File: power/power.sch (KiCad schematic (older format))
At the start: 69 parts, among them J1 Conn_01x02_Female, J10 Conn_01x02_Female, J11 Conn_01x02_Female, J12 Conn_01x02_Female, J13 Conn_01x02_Female, J14 Conn_01x02_Female, J15 Conn_01x03_Male, J2 Barrel_jack, J3 Conn_01x02_Female, J4 Conn_01x02_Female, J5 CONN_02X03, J6 Conn_01x02_Female, J7 Conn_01x02_Female, J8 Conn_01x02_Female, J9 Conn_01x02_Female, Q1 BS170, Q2 BS170, Q3 BS170, Q4 BS170, Q5 BS170, Q6 BS170, U1 ATMEGA16M1, U2 TPS2592xx, U3 LP5907MFX-3_3_NOPB

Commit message: final rev 1: nickel pads added and recovery footprint issues fixed
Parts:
- J1, J3, J4, J6, J7, J8: footprint Connector_PinHeader_1.00mm:PinHeader_1x02_P1.00mm_Vertical -> footprints:nickel_pad_bms
- sol1, sol2: footprint recovery-trigger-sp20:OSTTC030162 -> footprints:OSTTC030162
- tres1sol1, tres1sol2: footprint recovery-trigger-sp20:CSD16322Q5 -> footprints:TRANS_CSD17312Q5
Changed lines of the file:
@@
 F 0 "J1" H 5417 3116 50  0000 L CNN
 F 1 "Conn_01x02_Female" H 5417 3025 50  0000 L CNN
-F 2 "Connector_PinHeader_1.00mm:PinHeader_1x02_P1.00mm_Vertical" H 5390 3140 50  0001 C CNN
+F 2 "footprints:nickel_pad_bms" H 5390 3140 50  0001 C CNN
 F 3 "~" H 5390 3140 50  0001 C CNN
 	1    5390 3140
@@
 F 0 "J3" H 5427 3366 50  0000 L CNN
 F 1 "Conn_01x02_Female" H 5427 3275 50  0000 L CNN
-F 2 "Connector_PinHeader_1.00mm:PinHeader_1x02_P1.00mm_Vertical" H 5400 3390 50  0001 C CNN
+F 2 "footprints:nickel_pad_bms" H 5400 3390 50  0001 C CNN
 F 3 "~" H 5400 3390 50  0001 C CNN
 	1    5400 3390
@@
 F 0 "J4" H 5427 3606 50  0000 L CNN
 F 1 "Conn_01x02_Female" H 5427 3515 50  0000 L CNN
-F 2 "Connector_PinHeader_1.00mm:PinHeader_1x02_P1.00mm_Vertical" H 5400 3630 50  0001 C CNN
+F 2 "footprints:nickel_pad_bms" H 5400 3630 50  0001 C CNN
 F 3 "~" H 5400 3630 50  0001 C CNN
 	1    5400 3630
@@
 F 0 "J6" H 6277 3136 50  0000 L CNN
 F 1 "Conn_01x02_Female" H 6277 3045 50  0000 L CNN
-F 2 "Connector_PinHeader_1.00mm:PinHeader_1x02_P1.00mm_Vertical" H 6250 3160 50  0001 C CNN
+F 2 "footprints:nickel_pad_bms" H 6250 3160 50  0001 C CNN
 F 3 "~" H 6250 3160 50  0001 C CNN
 	1    6250 3160
@@
 F 0 "J7" H 6287 3376 50  0000 L CNN
 F 1 "Conn_01x02_Female" H 6287 3285 50  0000 L CNN
-F 2 "Connector_PinHeader_1.00mm:PinHeader_1x02_P1.00mm_Vertical" H 6260 3400 50  0001 C CNN
+F 2 "footprints:nickel_pad_bms" H 6260 3400 50  0001 C CNN
 F 3 "~" H 6260 3400 50  0001 C CNN
 	1    6260 3400
@@
 F 0 "J8" H 6287 3616 50  0000 L CNN
 F 1 "Conn_01x02_Female" H 6287 3525 50  0000 L CNN
-F 2 "Connector_PinHeader_1.00mm:PinHeader_1x02_P1.00mm_Vertical" H 6260 3640 50  0001 C CNN
+F 2 "footprints:nickel_pad_bms" H 6260 3640 50  0001 C CNN
 F 3 "~" H 6260 3640 50  0001 C CNN
 	1    6260 3640
@@
 F 0 "sol1" H 10172 2915 59  0000 C CNN
 F 1 "OSTTC03" H 10172 2810 59  0000 C CNN
-F 2 "recovery-trigger-sp20:OSTTC030162" H 10089 2669 59  0001 C CNN
+F 2 "footprints:OSTTC030162" H 10089 2669 59  0001 C CNN
 F 3 "http://www.on-shore.com/wp-content/uploads/OSTTCXX0162.pdf" H 10089 2669 59  0001 C CNN
 F 4 "https://www.digikey.com/product-detail/en/on-shore-technology-inc/OSTTC030162/ED2601-ND/614550" H 10189 2969 59  0001 C CNN "Purchasing Link"
@@
 F 0 "tres1sol1" H 13885 1394 50  0000 C CNN
 F 1 "NMOS_CDS16" H 13885 1303 50  0000 C CNN
-F 2 "recovery-trigger-sp20:CSD16322Q5" H 13085 1329 50  0001 C CNN
+F 2 "footprints:TRANS_CSD17312Q5" H 13085 1329 50  0001 C CNN
 F 3 "http://www.ti.com/general/docs/suppproductinfo.tsp?distId=10&gotoUrl=http%3A%2F%2Fwww.ti.com%2Flit%2Fgpn%2Fcsd16322q5" H 13985 1479 50  0001 C CNN
 F 4 "CSD16322Q5" H 14085 1629 50  0001 C CNN "MPN"
@@
 F 0 "tres1sol2" H 13936 3021 50  0000 C CNN
 F 1 "NMOS_CDS16" H 13936 2930 50  0000 C CNN
-F 2 "recovery-trigger-sp20:CSD16322Q5" H 13136 2956 50  0001 C CNN
+F 2 "footprints:TRANS_CSD17312Q5" H 13136 2956 50  0001 C CNN
 F 3 "http://www.ti.com/general/docs/suppproductinfo.tsp?distId=10&gotoUrl=http%3A%2F%2Fwww.ti.com%2Flit%2Fgpn%2Fcsd16322q5" H 14036 3106 50  0001 C CNN
 F 4 "CSD16322Q5" H 14136 3256 50  0001 C CNN "MPN"
@@
 F 0 "sol2" H 11374 2919 59  0000 C CNN
 F 1 "OSTTC03" H 11374 2814 59  0000 C CNN
-F 2 "recovery-trigger-sp20:OSTTC030162" H 11291 2673 59  0001 C CNN
+F 2 "footprints:OSTTC030162" H 11291 2673 59  0001 C CNN
 F 3 "http://www.on-shore.com/wp-content/uploads/OSTTCXX0162.pdf" H 11291 2673 59  0001 C CNN
 F 4 "https://www.digikey.com/product-detail/en/on-shore-technology-inc/OSTTC030162/ED2601-ND/614550" H 11391 2973 59  0001 C CNN "Purchasing Link"

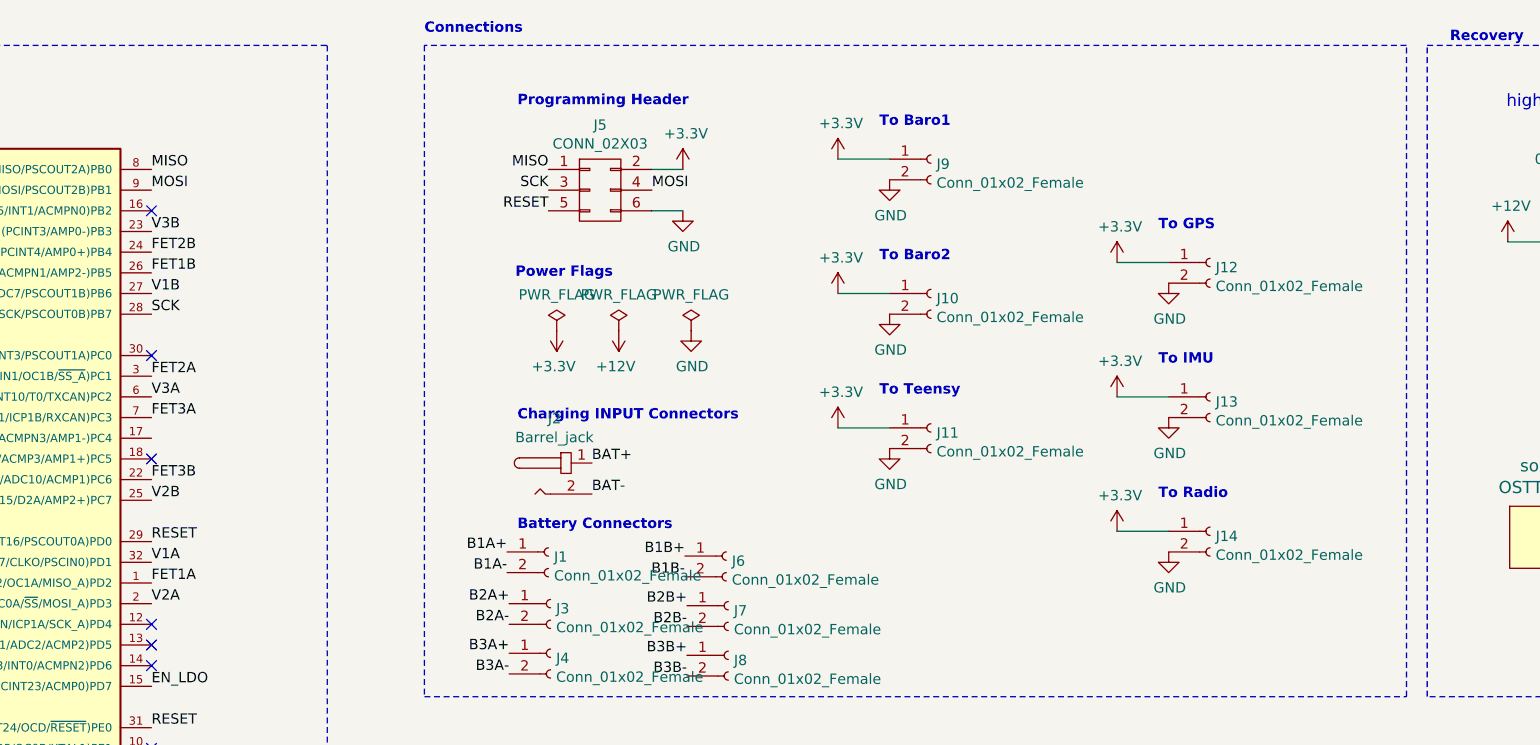
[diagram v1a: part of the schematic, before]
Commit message: ribbon added to sch and recovery wires increased and no connects added
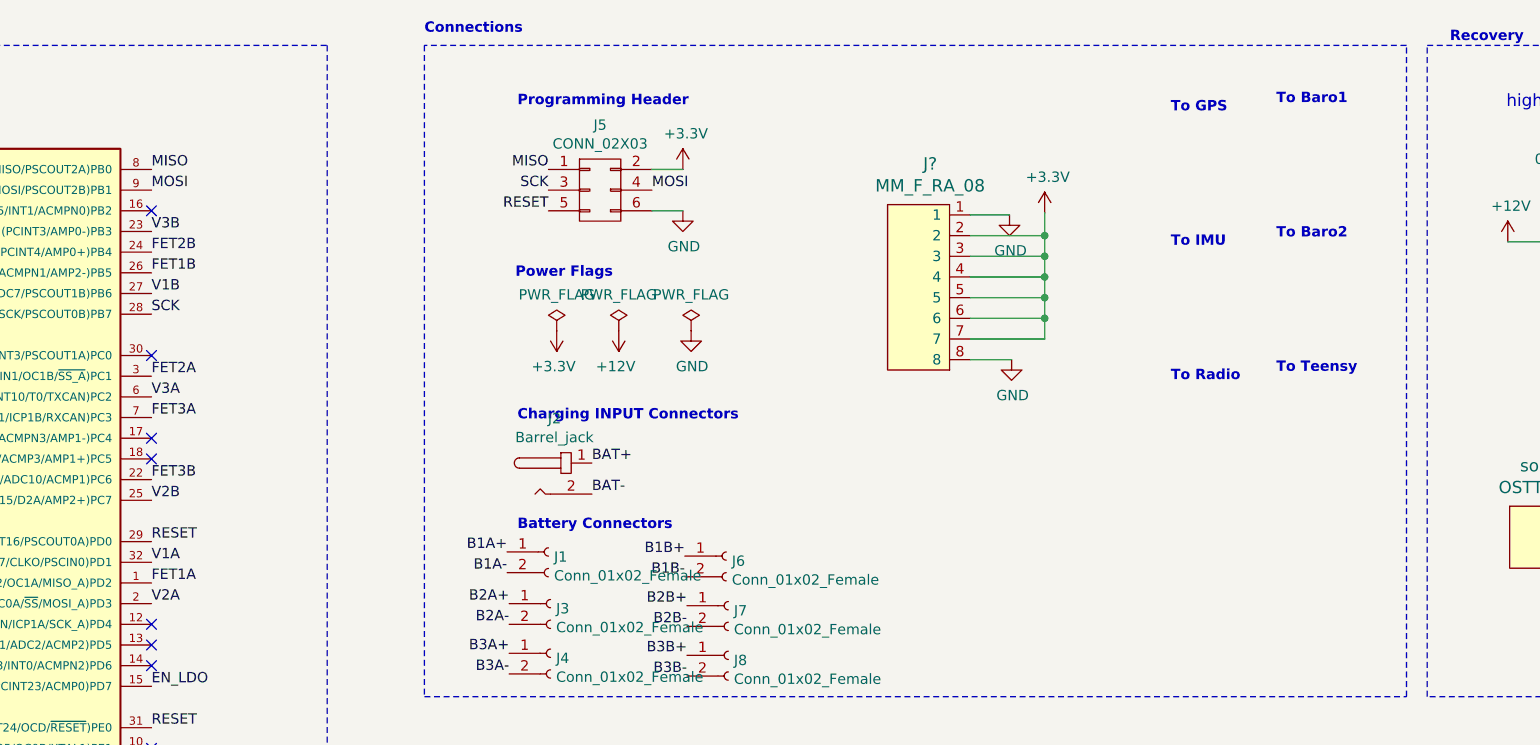
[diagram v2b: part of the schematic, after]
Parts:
- removed J10, J11, J12, J13, J14, J9: Conn_01x02_Female, Connector_PinHeader_1.00mm:PinHeader_1x02_P1.00mm_Vertical, symbol Connector:Conn_01x02_Female
- added J?: MM_F_RA_08, footprints:micromatch_female_ra_8, symbol rocketry:MM_F_RA_08
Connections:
- net +3V3: now also J?.2, J?.3, J?.4, J?.5, J?.6, J?.7
- net GND: now also J?.1, J?.8
- no-connect marks 8 -> 9

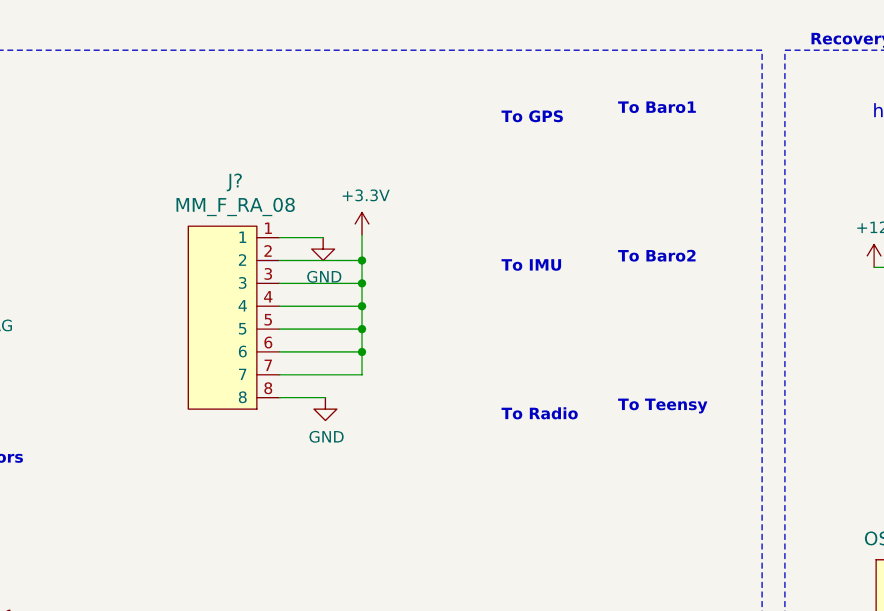
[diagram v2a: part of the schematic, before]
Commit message: complete bms - 0 drc errors, ribbon cable, pads not on edge
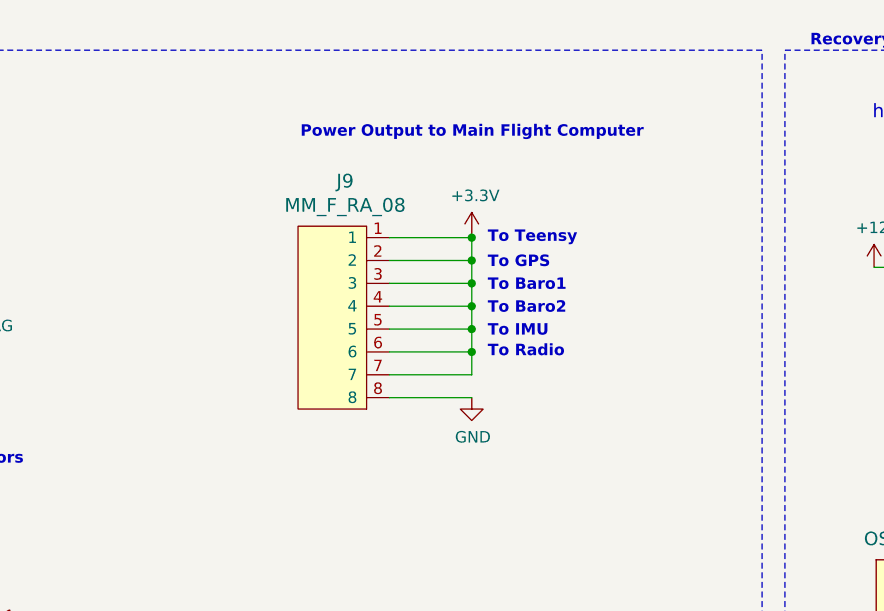
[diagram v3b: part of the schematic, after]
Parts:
- J1, J3, J4, J6, J7, J8: footprint footprints:nickel_pad_bms -> footprints:nickle_pads_1x2
- U2: footprint Package_SON:VSON-10-1EP_3x3mm_P0.5mm_EP1.65x2.4mm_ThermalVias -> footprints:VSON-10-1EP_3x3mm_P0.5mm_EP1.65x2.4mm_ThermalVias
- gave numbers to parts that had none: 1
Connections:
- net +3V3: now also J9.1
- net GND: no longer J9.1
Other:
- note added: "Power Output to Main Flight Computer"
- moved on the sheet: J9
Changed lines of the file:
@@
 F 0 "U2" H 7990 6038 50  0000 C CNN
 F 1 "TPS2592xx" H 7990 5947 50  0000 C CNN
-F 2 "Package_SON:VSON-10-1EP_3x3mm_P0.5mm_EP1.65x2.4mm_ThermalVias" H 7940 4910 50  0001 C CNN
+F 2 "footprints:VSON-10-1EP_3x3mm_P0.5mm_EP1.65x2.4mm_ThermalVias" H 7940 4910 50  0001 C CNN
 F 3 "http://www.ti.com/lit/ds/symlink/tps25925.pdf" H 7590 5960 50  0001 C CNN
 	1    7990 5560
@@
 	1    0    0    -1
 $EndComp
-Text Notes 8910 2280 0    50   ~ 10
+Text Notes 8340 1540 0    50   ~ 10
 To Teensy
 Text Notes 7240 5060 0    50   ~ 0
@@
 	1    0    0    -1
 $EndComp
-Text Notes 8910 1630 0    50   ~ 10
+Text Notes 8340 1850 0    50   ~ 10
 To Baro2
-Text Notes 8910 980  0    50   ~ 10
+Text Notes 8340 1750 0    50   ~ 10
 To Baro1
-Text Notes 8400 1670 0    50   ~ 10
+Text Notes 8340 1950 0    50   ~ 10
 To IMU
-Text Notes 8400 1020 0    50   ~ 10
+Text Notes 8340 1650 0    50   ~ 10
 To GPS
-Text Notes 8400 2320 0    50   ~ 10
+Text Notes 8340 2040 0    50   ~ 10
 To Radio
 $Comp
 L power:+3.3V #PWR0123
 U 1 1 5FF539A8
-P 7790 1500
-F 0 "#PWR0123" H 7790 1350 50  0001 C CNN
-F 1 "+3.3V" H 7805 1673 50  0000 C CNN
-F 2 "" H 7790 1500 50  0001 C CNN
-F 3 "" H 7790 1500 50  0001 C CNN
-	1    7790 1500
-	1    0    0    -1
-$EndComp
-$Comp
-L power:GND #PWR0124
-U 1 1 5FF539AF
-P 7620 1510
-F 0 "#PWR0124" H 7620 1260 50  0001 C CNN
-F 1 "GND" H 7625 1337 50  0000 C CNN
-F 2 "" H 7620 1510 50  0001 C CNN
-F 3 "" H 7620 1510 50  0001 C CNN
-	1    7620 1510
+P 8270 1500
+F 0 "#PWR0123" H 8270 1350 50  0001 C CNN
+F 1 "+3.3V" H 8285 1673 50  0000 C CNN
+F 2 "" H 8270 1500 50  0001 C CNN
+F 3 "" H 8270 1500 50  0001 C CNN
+	1    8270 1500
 	1    0    0    -1
 $EndComp
@@
 F 0 "J1" H 5417 3116 50  0000 L CNN
 F 1 "Conn_01x02_Female" H 5417 3025 50  0000 L CNN
-F 2 "footprints:nickel_pad_bms" H 5390 3140 50  0001 C CNN
+F 2 "footprints:nickle_pads_1x2" H 5390 3140 50  0001 C CNN
 F 3 "~" H 5390 3140 50  0001 C CNN
 	1    5390 3140
@@
 F 0 "J3" H 5427 3366 50  0000 L CNN
 F 1 "Conn_01x02_Female" H 5427 3275 50  0000 L CNN
-F 2 "footprints:nickel_pad_bms" H 5400 3390 50  0001 C CNN
+F 2 "footprints:nickle_pads_1x2" H 5400 3390 50  0001 C CNN
 F 3 "~" H 5400 3390 50  0001 C CNN
 	1    5400 3390
@@
 F 0 "J4" H 5427 3606 50  0000 L CNN
 F 1 "Conn_01x02_Female" H 5427 3515 50  0000 L CNN
-F 2 "footprints:nickel_pad_bms" H 5400 3630 50  0001 C CNN
+F 2 "footprints:nickle_pads_1x2" H 5400 3630 50  0001 C CNN
 F 3 "~" H 5400 3630 50  0001 C CNN
 	1    5400 3630
@@
 F 0 "J6" H 6277 3136 50  0000 L CNN
 F 1 "Conn_01x02_Female" H 6277 3045 50  0000 L CNN
-F 2 "footprints:nickel_pad_bms" H 6250 3160 50  0001 C CNN
+F 2 "footprints:nickle_pads_1x2" H 6250 3160 50  0001 C CNN
 F 3 "~" H 6250 3160 50  0001 C CNN
 	1    6250 3160
@@
 F 0 "J7" H 6287 3376 50  0000 L CNN
 F 1 "Conn_01x02_Female" H 6287 3285 50  0000 L CNN
-F 2 "footprints:nickel_pad_bms" H 6260 3400 50  0001 C CNN
+F 2 "footprints:nickle_pads_1x2" H 6260 3400 50  0001 C CNN
 F 3 "~" H 6260 3400 50  0001 C CNN
 	1    6260 3400
@@
 F 0 "J8" H 6287 3616 50  0000 L CNN
 F 1 "Conn_01x02_Female" H 6287 3525 50  0000 L CNN
-F 2 "footprints:nickel_pad_bms" H 6260 3640 50  0001 C CNN
+F 2 "footprints:nickle_pads_1x2" H 6260 3640 50  0001 C CNN
 F 3 "~" H 6260 3640 50  0001 C CNN
 	1    6260 3640
@@
 NoConn ~ 3470 2590
 $Comp
-L rocketry:MM_F_RA_08 J?
+L rocketry:MM_F_RA_08 J9
 U 1 1 5FFE5720
-P 7180 1810
-F 0 "J?" H 7236 2357 60  0000 C CNN
-F 1 "MM_F_RA_08" H 7236 2251 60  0000 C CNN
-F 2 "footprints:micromatch_female_ra_8" H 7080 2110 60  0001 C CNN
-F 3 "http://www.te.com/commerce/DocumentDelivery/DDEController?Action=showdoc&DocId=Customer+Drawing%7F338070%7FG1%7Fpdf%7FEnglish%7FENG_CD_338070_G1.pdf%7F338070-8" H 7180 2210 60  0001 C CNN
-F 4 "TE" H 7280 3210 60  0001 C CNN "MFN"
-F 5 "338070-8" H 7380 3310 60  0001 C CNN "MPN"
-F 6 "http://www.te.com/usa-en/product-338070-8.html" H 7280 2310 60  0001 C CNN "PurchasingLink"
-	1    7180 1810
-	1    0    0    -1
-$EndComp
-Wire Wire Line
-	7430 1610 7790 1610
-Wire Wire Line
-	7430 1710 7790 1710
-Wire Wire Line
-	7790 1710 7790 1610
-Connection ~ 7790 1610
-Wire Wire Line
-	7430 1810 7790 1810
-Wire Wire Line
-	7790 1810 7790 1710
-Connection ~ 7790 1710
-Wire Wire Line
-	7430 1910 7790 1910
-Wire Wire Line
-	7790 1910 7790 1810
-Connection ~ 7790 1810
-Wire Wire Line
-	7430 2010 7790 2010
-Wire Wire Line
-	7790 2010 7790 1910
-Connection ~ 7790 1910
-Wire Wire Line
-	7790 1500 7790 1610
-Wire Wire Line
-	7430 2110 7790 2110
-Wire Wire Line
-	7790 2110 7790 2010
-Connection ~ 7790 2010
-Wire Wire Line
-	7430 1510 7620 1510
-$Comp
-L power:GND #PWR?
-U 1 1 6003CE0A
-P 7630 2210
-F 0 "#PWR?" H 7630 1960 50  0001 C CNN
-F 1 "GND" H 7635 2037 50  0000 C CNN
-F 2 "" H 7630 2210 50  0001 C CNN
-F 3 "" H 7630 2210 50  0001 C CNN
-	1    7630 2210
-	1    0    0    -1
-$EndComp
-Wire Wire Line
-	7430 2210 7630 2210
+P 7660 1810
+F 0 "J9" H 7716 2357 60  0000 C CNN
+F 1 "MM_F_RA_08" H 7716 2251 60  0000 C CNN
+F 2 "footprints:micromatch_female_ra_8" H 7560 2110 60  0001 C CNN
+F 3 "http://www.te.com/commerce/DocumentDelivery/DDEController?Action=showdoc&DocId=Customer+Drawing%7F338070%7FG1%7Fpdf%7FEnglish%7FENG_CD_338070_G1.pdf%7F338070-8" H 7660 2210 60  0001 C CNN
+F 4 "TE" H 7760 3210 60  0001 C CNN "MFN"
+F 5 "338070-8" H 7860 3310 60  0001 C CNN "MPN"
+F 6 "http://www.te.com/usa-en/product-338070-8.html" H 7760 2310 60  0001 C CNN "PurchasingLink"
+	1    7660 1810
+	1    0    0    -1
+$EndComp
+Wire Wire Line
+	7910 1610 8270 1610
+Wire Wire Line
+	7910 1710 8270 1710
+Wire Wire Line
+	8270 1710 8270 1610
+Connection ~ 8270 1610
+Wire Wire Line
+	7910 1810 8270 1810
+Wire Wire Line
+	8270 1810 8270 1710
+Connection ~ 8270 1710
+Wire Wire Line
+	7910 1910 8270 1910
+Wire Wire Line
+	8270 1910 8270 1810
+Connection ~ 8270 1810
+Wire Wire Line
+	7910 2010 8270 2010
+Wire Wire Line
+	8270 2010 8270 1910
+Connection ~ 8270 1910
+Wire Wire Line
+	8270 1500 8270 1510
+Wire Wire Line
+	7910 2110 8270 2110
+Wire Wire Line
+	8270 2110 8270 2010
+Connection ~ 8270 2010
+Wire Wire Line
+	7910 1510 8270 1510
+Connection ~ 8270 1510
+Wire Wire Line
+	8270 1510 8270 1610
+Wire Wire Line
+	7910 2210 8270 2210
+$Comp
+L power:GND #PWR0111
+U 1 1 6006DD5A
+P 8270 2210
+F 0 "#PWR0111" H 8270 1960 50  0001 C CNN
+F 1 "GND" H 8275 2037 50  0000 C CNN
+F 2 "" H 8270 2210 50  0001 C CNN
+F 3 "" H 8270 2210 50  0001 C CNN
+	1    8270 2210
+	1    0    0    -1
+$EndComp
+Text Notes 7520 1080 0    50   ~ 10
+Power Output to Main Flight Computer
 $EndSCHEMATC

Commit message: Add new gerbers
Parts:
- D3: symbol formula:D_Zener_13V -> power-rescue:D_Zener_13V-formula
- D4: symbol formula:LED_0805_Red -> power-rescue:LED_0805_Red-formula
- D5: symbol formula:LED_0805_Amber -> power-rescue:LED_0805_Amber-formula
- J2: symbol formula:Barrel_jack -> power-rescue:Barrel_jack-formula
- J5: symbol formula:CONN_02X03 -> power-rescue:CONN_02X03-formula
- U1: symbol formula:ATMEGA16M1 -> power-rescue:ATMEGA16M1-formula
- U3: symbol dk_PMIC-Voltage-Regulators-Linear:LP5907MFX-3_3_NOPB -> power-rescue:LP5907MFX-3_3_NOPB-dk_PMIC-Voltage-Regulators-Linear
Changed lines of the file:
@@
 EESchema Schematic File Version 4
 LIBS:power
+LIBS:device
 LIBS:74xx
+LIBS:audio
+LIBS:interface
 LIBS:power-cache
-EELAYER 26 0
+EELAYER 30 0
 EELAYER END
 $Descr A3 16535 11693
@@
 	1140 6410 1140 6460
 $Comp
-L formula:CONN_02X03 J5
+L power-rescue:CONN_02X03-formula J5
 U 1 1 5E15A020
 P 5640 1390
@@
 Step Down Circuitry
 $Comp
-L dk_PMIC-Voltage-Regulators-Linear:LP5907MFX-3_3_NOPB U3
+L power-rescue:LP5907MFX-3_3_NOPB-dk_PMIC-Voltage-Regulators-Linear U3
 U 1 1 5FD3AE30
 P 10690 5580
@@
 Connection ~ 1270 1590
 $Comp
-L formula:ATMEGA16M1 U1
+L power-rescue:ATMEGA16M1-formula U1
 U 1 1 5FC49FC2
 P 2370 2990
@@
 BAT-
 $Comp
-L formula:Barrel_jack J2
+L power-rescue:Barrel_jack-formula J2
 U 1 1 5FF50D05
 P 5400 2510
@@
 $EndComp
 $Comp
-L formula:D_Zener_13V D3
+L power-rescue:D_Zener_13V-formula D3
 U 1 1 5FF6B278
 P 5990 7410
@@
 $EndComp
 $Comp
-L formula:LED_0805_Red D4
+L power-rescue:LED_0805_Red-formula D4
 U 1 1 600CFD2B
 P 13500 5560
@@
 $EndComp
 $Comp
-L formula:LED_0805_Amber D5
+L power-rescue:LED_0805_Amber-formula D5
 U 1 1 600F0E83
 P 14300 5560
